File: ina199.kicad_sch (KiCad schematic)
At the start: 4 parts, among them J41 Conn_02x03_Odd_Even, U22 INA199A1DCKR

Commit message: WIP v0.2.0 changes
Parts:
- J36: renamed from J41; value Conn_02x03_Odd_Even -> Conn_01x03; footprint HL_Connector_Pad_2.54mm:Pad_2x03_P2.54_1.7x1.7_Rect-Oct -> HL_Connector_Pad_2.54mm:Pad_1x03_P2.54_1.7x1.7_Oct; symbol Connector_Generic:Conn_02x03_Odd_Even -> Connector_Generic:Conn_01x03
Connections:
- net GND: no longer J36.1 (Pin_1), J36.3 (Pin_3), J36.5 (Pin_5)
- net IN1: now also J36.1 (Pin_1); no longer J36.2 (Pin_2)
- net OUT1: now also J36.2 (Pin_2); no longer J36.4 (Pin_4)
- net V1: now also J36.3 (Pin_3); no longer J36.6 (Pin_6)

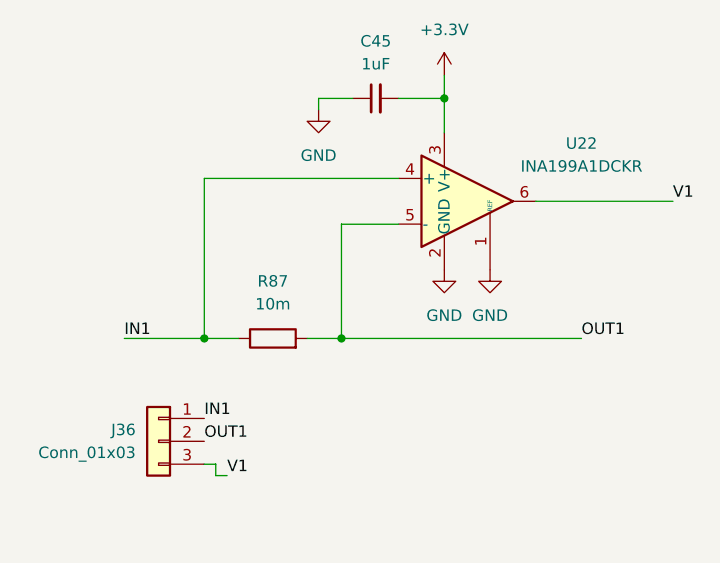
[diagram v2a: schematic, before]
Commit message: Assign part numbers and finish other 0.2.0 changes
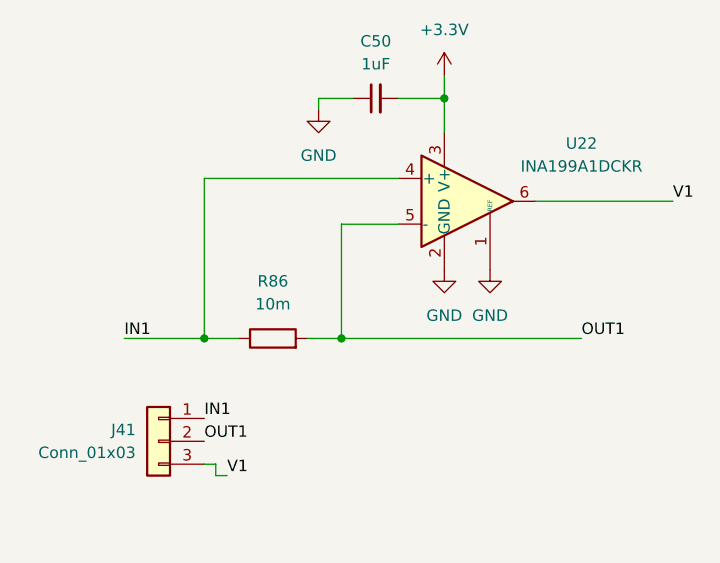
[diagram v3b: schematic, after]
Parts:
- J41: renamed from J36; LCSC (none) -> C2937625
- renumbered C45 to C50, R87 to R86
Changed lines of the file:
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@@
 		(dnp no)
 		(fields_autoplaced yes)
-		(property "Reference" "#PWR0173"
+		(property "Reference" "#PWR0183"
 			(at 144.78 68.58 0)
 			(effects
@@
 			(project "HALSPA"
 				(path "/7eeba806-440e-4671-bc07-69fe183910a7/2f123bd3-5a8a-4eda-a345-37c747287444/4af25350-e1ae-4cb6-8ebc-d8cb232dd08c"
-					(reference "#PWR0231")
-					(unit 1)
-				)
-				(path "/7eeba806-440e-4671-bc07-69fe183910a7/2f123bd3-5a8a-4eda-a345-37c747287444/622497c5-aad0-4b8f-b029-b557d24d2703"
-					(reference "#PWR0211")
-					(unit 1)
-				)
-				(path "/7eeba806-440e-4671-bc07-69fe183910a7/2f123bd3-5a8a-4eda-a345-37c747287444/77ced212-f85d-4df5-9c9d-672ca2ee0ad7"
-					(reference "#PWR0173")
-					(unit 1)
-				)
-				(path "/7eeba806-440e-4671-bc07-69fe183910a7/2f123bd3-5a8a-4eda-a345-37c747287444/ce058287-6d95-4419-af16-33ee4d22930e"
-					(reference "#PWR0187")
+					(reference "#PWR0237")
+					(unit 1)
+				)
+				(path "/7eeba806-440e-4671-bc07-69fe183910a7/2f123bd3-5a8a-4eda-a345-37c747287444/622497c5-aad0-4b8f-b029-b557d24d2703"
+					(reference "#PWR0220")
+					(unit 1)
+				)
+				(path "/7eeba806-440e-4671-bc07-69fe183910a7/2f123bd3-5a8a-4eda-a345-37c747287444/77ced212-f85d-4df5-9c9d-672ca2ee0ad7"
+					(reference "#PWR0183")
+					(unit 1)
+				)
+				(path "/7eeba806-440e-4671-bc07-69fe183910a7/2f123bd3-5a8a-4eda-a345-37c747287444/ce058287-6d95-4419-af16-33ee4d22930e"
+					(reference "#PWR0198")
 					(unit 1)
 				)
@@
 		(dnp no)
 		(fields_autoplaced yes)
-		(property "Reference" "#PWR0175"
+		(property "Reference" "#PWR0185"
 			(at 149.86 92.71 0)
 			(effects
@@
 			(project "HALSPA"
 				(path "/7eeba806-440e-4671-bc07-69fe183910a7/2f123bd3-5a8a-4eda-a345-37c747287444/4af25350-e1ae-4cb6-8ebc-d8cb232dd08c"
-					(reference "#PWR0233")
-					(unit 1)
-				)
-				(path "/7eeba806-440e-4671-bc07-69fe183910a7/2f123bd3-5a8a-4eda-a345-37c747287444/622497c5-aad0-4b8f-b029-b557d24d2703"
-					(reference "#PWR0213")
-					(unit 1)
-				)
-				(path "/7eeba806-440e-4671-bc07-69fe183910a7/2f123bd3-5a8a-4eda-a345-37c747287444/77ced212-f85d-4df5-9c9d-672ca2ee0ad7"
-					(reference "#PWR0175")
-					(unit 1)
-				)
-				(path "/7eeba806-440e-4671-bc07-69fe183910a7/2f123bd3-5a8a-4eda-a345-37c747287444/ce058287-6d95-4419-af16-33ee4d22930e"
-					(reference "#PWR0189")
+					(reference "#PWR0239")
+					(unit 1)
+				)
+				(path "/7eeba806-440e-4671-bc07-69fe183910a7/2f123bd3-5a8a-4eda-a345-37c747287444/622497c5-aad0-4b8f-b029-b557d24d2703"
+					(reference "#PWR0222")
+					(unit 1)
+				)
+				(path "/7eeba806-440e-4671-bc07-69fe183910a7/2f123bd3-5a8a-4eda-a345-37c747287444/77ced212-f85d-4df5-9c9d-672ca2ee0ad7"
+					(reference "#PWR0185")
+					(unit 1)
+				)
+				(path "/7eeba806-440e-4671-bc07-69fe183910a7/2f123bd3-5a8a-4eda-a345-37c747287444/ce058287-6d95-4419-af16-33ee4d22930e"
+					(reference "#PWR0200")
 					(unit 1)
 				)
@@
 		(dnp no)
 		(fields_autoplaced yes)
-		(property "Reference" "#PWR0174"
+		(property "Reference" "#PWR0184"
 			(at 144.78 92.71 0)
 			(effects
@@
 			(project "HALSPA"
 				(path "/7eeba806-440e-4671-bc07-69fe183910a7/2f123bd3-5a8a-4eda-a345-37c747287444/4af25350-e1ae-4cb6-8ebc-d8cb232dd08c"
-					(reference "#PWR0232")
-					(unit 1)
-				)
-				(path "/7eeba806-440e-4671-bc07-69fe183910a7/2f123bd3-5a8a-4eda-a345-37c747287444/622497c5-aad0-4b8f-b029-b557d24d2703"
-					(reference "#PWR0212")
-					(unit 1)
-				)
-				(path "/7eeba806-440e-4671-bc07-69fe183910a7/2f123bd3-5a8a-4eda-a345-37c747287444/77ced212-f85d-4df5-9c9d-672ca2ee0ad7"
-					(reference "#PWR0174")
-					(unit 1)
-				)
-				(path "/7eeba806-440e-4671-bc07-69fe183910a7/2f123bd3-5a8a-4eda-a345-37c747287444/ce058287-6d95-4419-af16-33ee4d22930e"
-					(reference "#PWR0188")
+					(reference "#PWR0238")
+					(unit 1)
+				)
+				(path "/7eeba806-440e-4671-bc07-69fe183910a7/2f123bd3-5a8a-4eda-a345-37c747287444/622497c5-aad0-4b8f-b029-b557d24d2703"
+					(reference "#PWR0221")
+					(unit 1)
+				)
+				(path "/7eeba806-440e-4671-bc07-69fe183910a7/2f123bd3-5a8a-4eda-a345-37c747287444/77ced212-f85d-4df5-9c9d-672ca2ee0ad7"
+					(reference "#PWR0184")
+					(unit 1)
+				)
+				(path "/7eeba806-440e-4671-bc07-69fe183910a7/2f123bd3-5a8a-4eda-a345-37c747287444/ce058287-6d95-4419-af16-33ee4d22930e"
+					(reference "#PWR0199")
 					(unit 1)
 				)
@@
 		(dnp no)
 		(fields_autoplaced yes)
-		(property "Reference" "C45"
+		(property "Reference" "C50"
 			(at 137.1663 60.96 90)
 			(effects
@@
 			(project "HALSPA"
 				(path "/7eeba806-440e-4671-bc07-69fe183910a7/2f123bd3-5a8a-4eda-a345-37c747287444/4af25350-e1ae-4cb6-8ebc-d8cb232dd08c"
+					(reference "C63")
+					(unit 1)
+				)
+				(path "/7eeba806-440e-4671-bc07-69fe183910a7/2f123bd3-5a8a-4eda-a345-37c747287444/622497c5-aad0-4b8f-b029-b557d24d2703"
 					(reference "C58")
 					(unit 1)
 				)
-				(path "/7eeba806-440e-4671-bc07-69fe183910a7/2f123bd3-5a8a-4eda-a345-37c747287444/622497c5-aad0-4b8f-b029-b557d24d2703"
-					(reference "C53")
-					(unit 1)
-				)
-				(path "/7eeba806-440e-4671-bc07-69fe183910a7/2f123bd3-5a8a-4eda-a345-37c747287444/77ced212-f85d-4df5-9c9d-672ca2ee0ad7"
-					(reference "C45")
-					(unit 1)
-				)
-				(path "/7eeba806-440e-4671-bc07-69fe183910a7/2f123bd3-5a8a-4eda-a345-37c747287444/ce058287-6d95-4419-af16-33ee4d22930e"
-					(reference "C47")
+				(path "/7eeba806-440e-4671-bc07-69fe183910a7/2f123bd3-5a8a-4eda-a345-37c747287444/77ced212-f85d-4df5-9c9d-672ca2ee0ad7"
+					(reference "C50")
+					(unit 1)
+				)
+				(path "/7eeba806-440e-4671-bc07-69fe183910a7/2f123bd3-5a8a-4eda-a345-37c747287444/ce058287-6d95-4419-af16-33ee4d22930e"
+					(reference "C52")
 					(unit 1)
 				)
@@
 		(dnp no)
 		(fields_autoplaced yes)
-		(property "Reference" "#PWR0172"
+		(property "Reference" "#PWR0182"
 			(at 130.81 74.93 0)
 			(effects
@@
 			(project "HALSPA"
 				(path "/7eeba806-440e-4671-bc07-69fe183910a7/2f123bd3-5a8a-4eda-a345-37c747287444/4af25350-e1ae-4cb6-8ebc-d8cb232dd08c"
-					(reference "#PWR0230")
-					(unit 1)
-				)
-				(path "/7eeba806-440e-4671-bc07-69fe183910a7/2f123bd3-5a8a-4eda-a345-37c747287444/622497c5-aad0-4b8f-b029-b557d24d2703"
-					(reference "#PWR0210")
-					(unit 1)
-				)
-				(path "/7eeba806-440e-4671-bc07-69fe183910a7/2f123bd3-5a8a-4eda-a345-37c747287444/77ced212-f85d-4df5-9c9d-672ca2ee0ad7"
-					(reference "#PWR0172")
-					(unit 1)
-				)
-				(path "/7eeba806-440e-4671-bc07-69fe183910a7/2f123bd3-5a8a-4eda-a345-37c747287444/ce058287-6d95-4419-af16-33ee4d22930e"
-					(reference "#PWR0186")
+					(reference "#PWR0236")
+					(unit 1)
+				)
+				(path "/7eeba806-440e-4671-bc07-69fe183910a7/2f123bd3-5a8a-4eda-a345-37c747287444/622497c5-aad0-4b8f-b029-b557d24d2703"
+					(reference "#PWR0219")
+					(unit 1)
+				)
+				(path "/7eeba806-440e-4671-bc07-69fe183910a7/2f123bd3-5a8a-4eda-a345-37c747287444/77ced212-f85d-4df5-9c9d-672ca2ee0ad7"
+					(reference "#PWR0182")
+					(unit 1)
+				)
+				(path "/7eeba806-440e-4671-bc07-69fe183910a7/2f123bd3-5a8a-4eda-a345-37c747287444/ce058287-6d95-4419-af16-33ee4d22930e"
+					(reference "#PWR0197")
 					(unit 1)
 				)
@@
 		(dnp no)
 		(fields_autoplaced yes)
-		(property "Reference" "R87"
+		(property "Reference" "R86"
 			(at 125.73 87.63 90)
 			(effects
@@
 			(project "HALSPA"
 				(path "/7eeba806-440e-4671-bc07-69fe183910a7/2f123bd3-5a8a-4eda-a345-37c747287444/4af25350-e1ae-4cb6-8ebc-d8cb232dd08c"
-					(reference "R111")
-					(unit 1)
-				)
-				(path "/7eeba806-440e-4671-bc07-69fe183910a7/2f123bd3-5a8a-4eda-a345-37c747287444/622497c5-aad0-4b8f-b029-b557d24d2703"
-					(reference "R109")
-					(unit 1)
-				)
-				(path "/7eeba806-440e-4671-bc07-69fe183910a7/2f123bd3-5a8a-4eda-a345-37c747287444/77ced212-f85d-4df5-9c9d-672ca2ee0ad7"
+					(reference "R110")
+					(unit 1)
+				)
+				(path "/7eeba806-440e-4671-bc07-69fe183910a7/2f123bd3-5a8a-4eda-a345-37c747287444/622497c5-aad0-4b8f-b029-b557d24d2703"
+					(reference "R108")
+					(unit 1)
+				)
+				(path "/7eeba806-440e-4671-bc07-69fe183910a7/2f123bd3-5a8a-4eda-a345-37c747287444/77ced212-f85d-4df5-9c9d-672ca2ee0ad7"
+					(reference "R86")
+					(unit 1)
+				)
+				(path "/7eeba806-440e-4671-bc07-69fe183910a7/2f123bd3-5a8a-4eda-a345-37c747287444/ce058287-6d95-4419-af16-33ee4d22930e"
 					(reference "R87")
-					(unit 1)
-				)
-				(path "/7eeba806-440e-4671-bc07-69fe183910a7/2f123bd3-5a8a-4eda-a345-37c747287444/ce058287-6d95-4419-af16-33ee4d22930e"
-					(reference "R88")
 					(unit 1)
 				)
@@
 		(on_board yes)
 		(dnp no)
-		(property "Reference" "J36"
+		(property "Reference" "J41"
 			(at 110.49 104.1399 0)
 			(effects
@@
 			)
 		)
+		(property "LCSC" "C2937625"
+			(at 113.03 105.41 0)
+			(effects
+				(font
+					(size 1.27 1.27)
+				)
+				(hide yes)
+			)
+		)
 		(pin "1"
 		)
@@
 			(project "HALSPA"
 				(path "/7eeba806-440e-4671-bc07-69fe183910a7/2f123bd3-5a8a-4eda-a345-37c747287444/4af25350-e1ae-4cb6-8ebc-d8cb232dd08c"
-					(reference "J53")
-					(unit 1)
-				)
-				(path "/7eeba806-440e-4671-bc07-69fe183910a7/2f123bd3-5a8a-4eda-a345-37c747287444/622497c5-aad0-4b8f-b029-b557d24d2703"
+					(reference "J59")
+					(unit 1)
+				)
+				(path "/7eeba806-440e-4671-bc07-69fe183910a7/2f123bd3-5a8a-4eda-a345-37c747287444/622497c5-aad0-4b8f-b029-b557d24d2703"
+					(reference "J55")
+					(unit 1)
+				)
+				(path "/7eeba806-440e-4671-bc07-69fe183910a7/2f123bd3-5a8a-4eda-a345-37c747287444/77ced212-f85d-4df5-9c9d-672ca2ee0ad7"
+					(reference "J41")
+					(unit 1)
+				)
+				(path "/7eeba806-440e-4671-bc07-69fe183910a7/2f123bd3-5a8a-4eda-a345-37c747287444/ce058287-6d95-4419-af16-33ee4d22930e"
 					(reference "J48")
 					(unit 1)
 				)
-				(path "/7eeba806-440e-4671-bc07-69fe183910a7/2f123bd3-5a8a-4eda-a345-37c747287444/77ced212-f85d-4df5-9c9d-672ca2ee0ad7"
-					(reference "J36")
-					(unit 1)
-				)
-				(path "/7eeba806-440e-4671-bc07-69fe183910a7/2f123bd3-5a8a-4eda-a345-37c747287444/ce058287-6d95-4419-af16-33ee4d22930e"
-					(reference "J41")
-					(unit 1)
-				)

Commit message: Update the title blocks
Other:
- company: (none) -> Hat Labs Oy
- title: (none) -> HALSPA - Hat Labs Spaghetti Board
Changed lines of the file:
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@@
 	(generator_version "9.0")
 	(paper "A4")
+	(title_block
+		(title "HALSPA - Hat Labs Spaghetti Board")
+		(date "2025-04-17")
+		(rev "v0.2.0")
+		(company "Hat Labs Oy")
+		(comment 1 "See the accompanying LICENSE.md file for license details.")
+	)
 	(junction
 		(at 144.78 67.31)

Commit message: Add JLCPCB corrections
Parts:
- J41: JLCPCB_CORRECTION (none) -> 0;2.54;270
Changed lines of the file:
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@@
+			)
+		)
+		(property "JLCPCB_CORRECTION" "0;2.54;270"
+			(at 113.03 105.41 0)
+			(effects
+				(font
+					(size 1.27 1.27)
+				)
+				(hide yes)
 			)
 		)

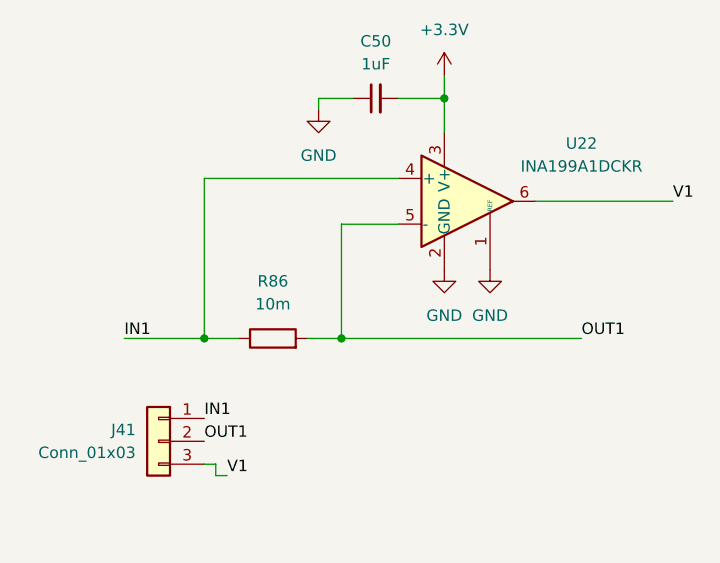
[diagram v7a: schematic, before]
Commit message: Update the design to a stackable one
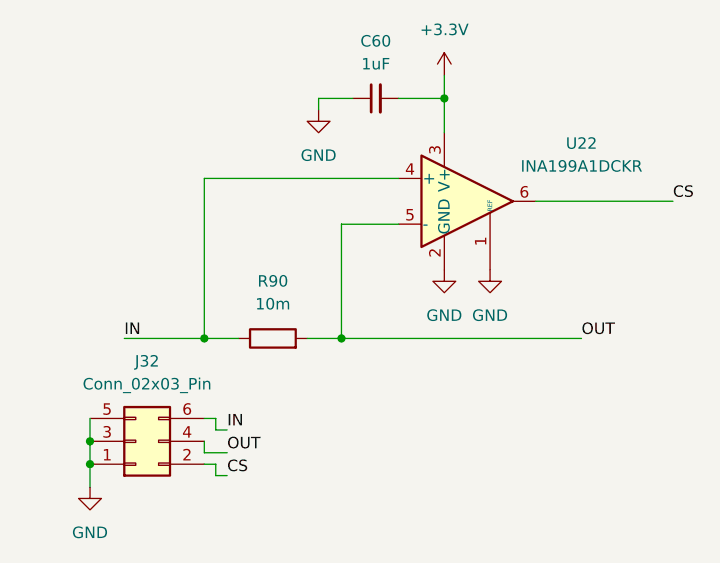
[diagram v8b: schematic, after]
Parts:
- J32: renamed from J41; value Conn_01x03 -> Conn_02x03_Pin; footprint HL_Connector_Pad_2.54mm:Pad_1x03_P2.54_1.7x1.7_Oct -> HL_Connector_Pad_2.54mm:Pad_2x03_P2.54_1.7x1.7_Rect-1Oct-2Rnd; symbol Connector_Generic:Conn_01x03 -> Connector_Generic:Conn_02x03_Odd_Even; JLCPCB_CORRECTION 0;2.54;270 -> 1.27;-2.54;270; LCSC C2937625 -> C2685197
- renumbered C50 to C60, R86 to R90
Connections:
- net GND: now also J32.1 (Pin_1), J32.3 (Pin_3), J32.5 (Pin_5)
- net IN1 renamed IN
- net IN: now also J32.6 (Pin_6); no longer J32.1 (Pin_1)
- net OUT1 renamed OUT
- net OUT: now also J32.4 (Pin_4); no longer J32.2 (Pin_2)
- net V1 renamed CS
- net CS: now also J32.2 (Pin_2); no longer J32.3 (Pin_3)
